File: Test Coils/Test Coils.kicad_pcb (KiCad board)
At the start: 2 copper layers, 71.7 x 64.6 mm, 6 parts, among them J1 Conn_01x02, J2 Conn_01x02, J3 Conn_01x02

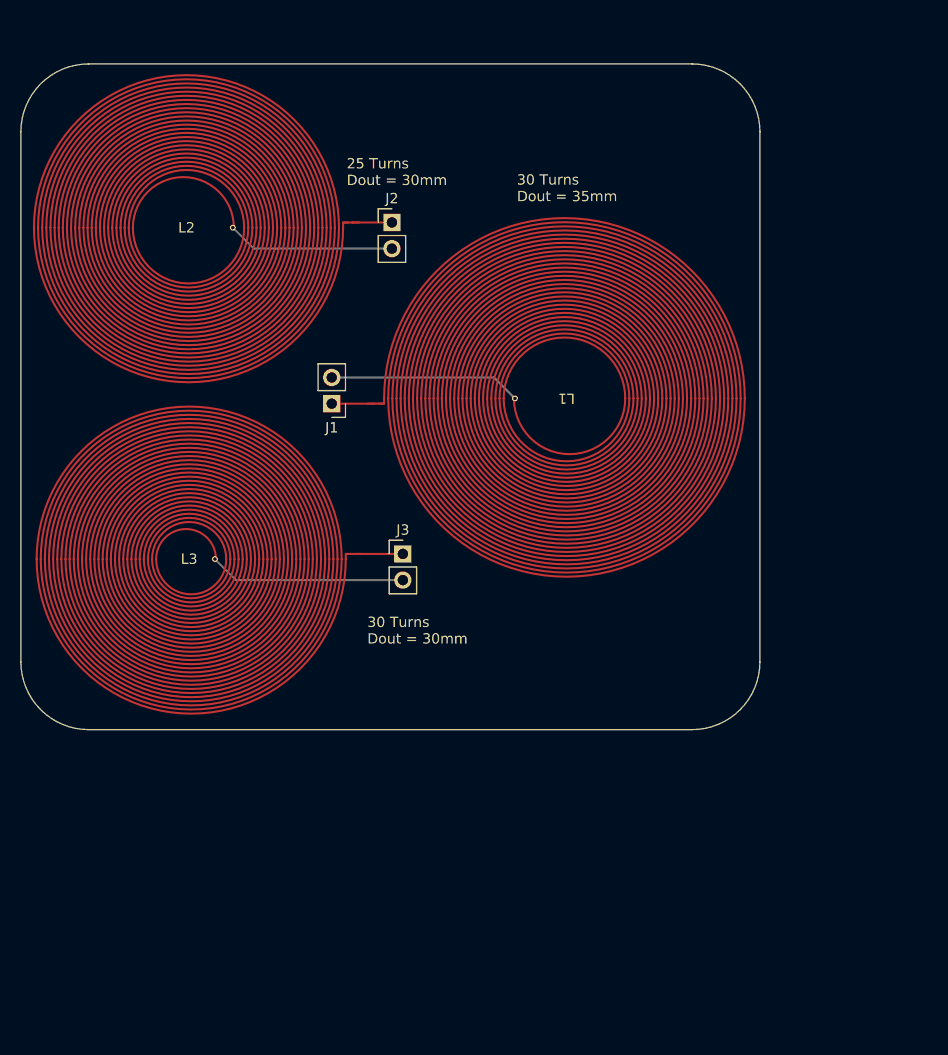
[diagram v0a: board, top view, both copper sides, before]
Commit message: feat(hw): panelizing
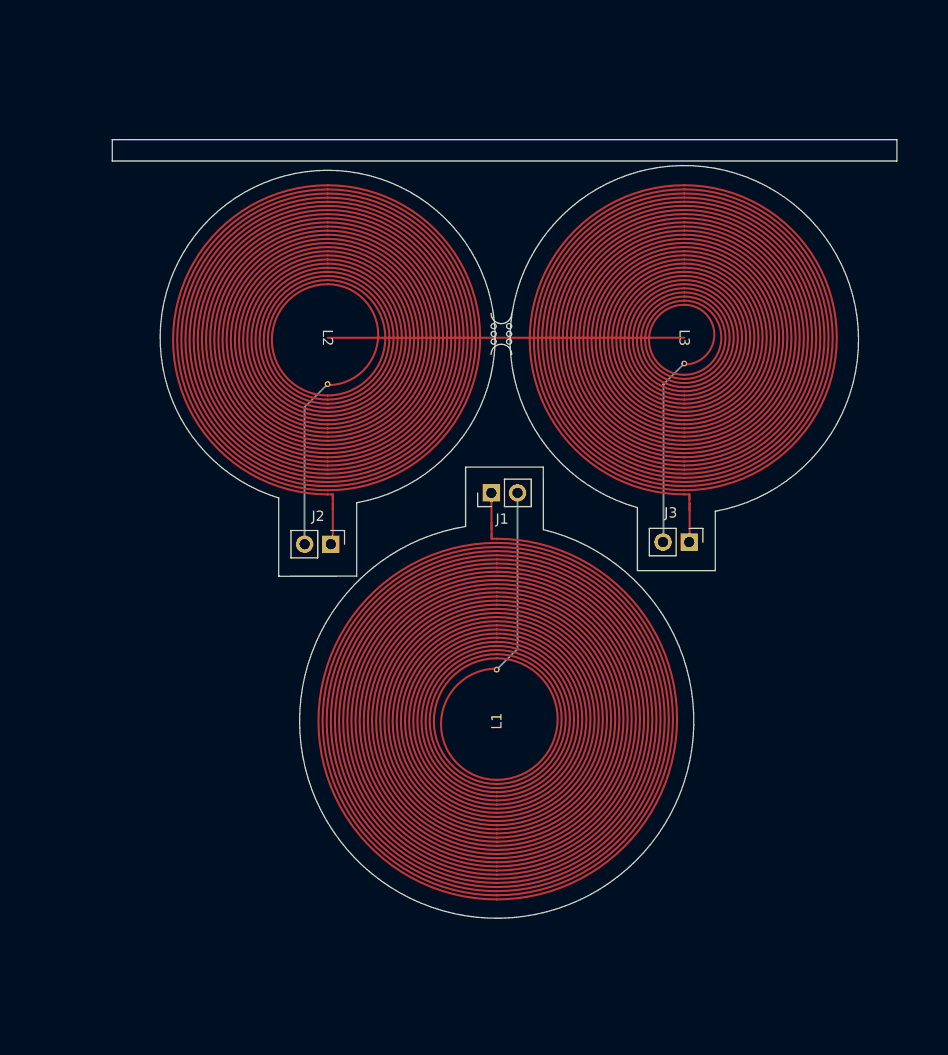
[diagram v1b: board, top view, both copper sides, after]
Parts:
- added mouse-bite-2mm-slot: VAL**, Panelization:mouse-bite-2mm-slot, F.Cu at (60.9, 42.5)
- moved L3 52.6 mm to (78.7, 42.9), turned to -90 degrees
- moved L1 32.0 mm to (60.5, 80.1), turned to 90 degrees
- moved J2 31.8 mm to (44.4, 62.9), turned to -90 degrees
- moved J3 27.8 mm to (79.1, 62.7), turned to -90 degrees
- moved J1 17.7 mm to (59.9, 57.9), turned to 90 degrees
- moved L2 17.4 mm to (44.0, 42.9), turned to -90 degrees
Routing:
- net Net-(J3-Pin_2): track 19.1 -> 18.2 mm
- net Net-(J3-Pin_1): track 4.64 -> 3.76 mm
- net Net-(J1-Pin_1): track 4.17 -> 3.54 mm
- net Net-(J1-Pin_2): track 18.6 -> 18.0 mm
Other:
- board size 71.7 x 64.6 mm -> 76.1 x 75.6 mm

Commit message: fix(hw): change edge cuts
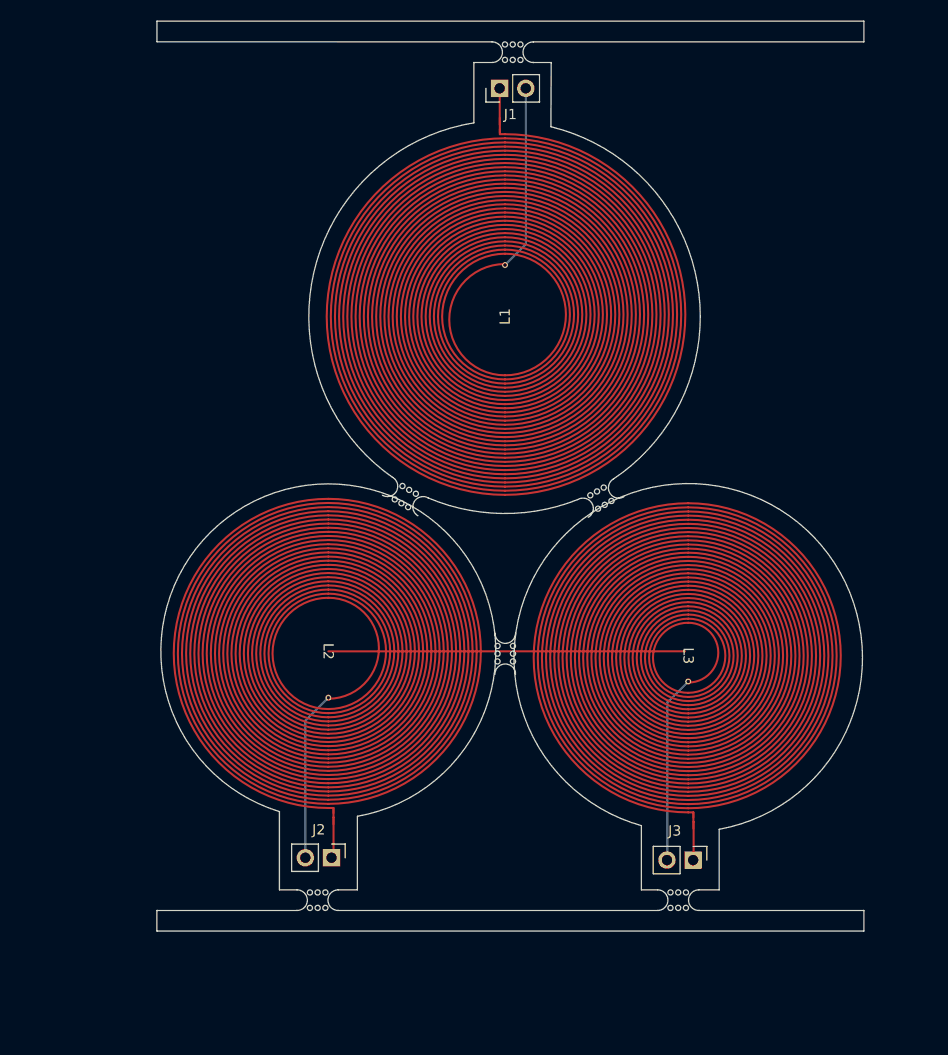
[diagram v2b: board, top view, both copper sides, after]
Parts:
- added mouse-bite-2mm-slot: VAL**, Panelization:mouse-bite-2mm-slot, F.Cu at (43.1, 97.5)
- added mouse-bite-2mm-slot: VAL**, Panelization:mouse-bite-2mm-slot, F.Cu at (70.6, 58.4)
- added mouse-bite-2mm-slot: VAL**, Panelization:mouse-bite-2mm-slot, F.Cu at (62.0, 15.2)
- added mouse-bite-2mm-slot: VAL**, Panelization:mouse-bite-2mm-slot, F.Cu at (51.6, 58.3)
- added mouse-bite-2mm-slot: VAL**, Panelization:mouse-bite-2mm-slot, F.Cu at (78.1, 97.5)
- moved J1 39.3 mm to (60.7, 18.7)
- moved L1 39.3 mm to (61.3, 40.8)
- moved mouse-bite-2mm-slot 31.0 mm to (61.3, 73.5)
- moved L3 30.9 mm to (79.0, 73.7)
- moved J3 30.9 mm to (79.5, 93.6)
- moved J2 30.4 mm to (44.4, 93.3)
- moved L2 30.4 mm to (44.1, 73.3)
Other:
- board size 76.1 x 75.6 mm -> 68.6 x 88.3 mm

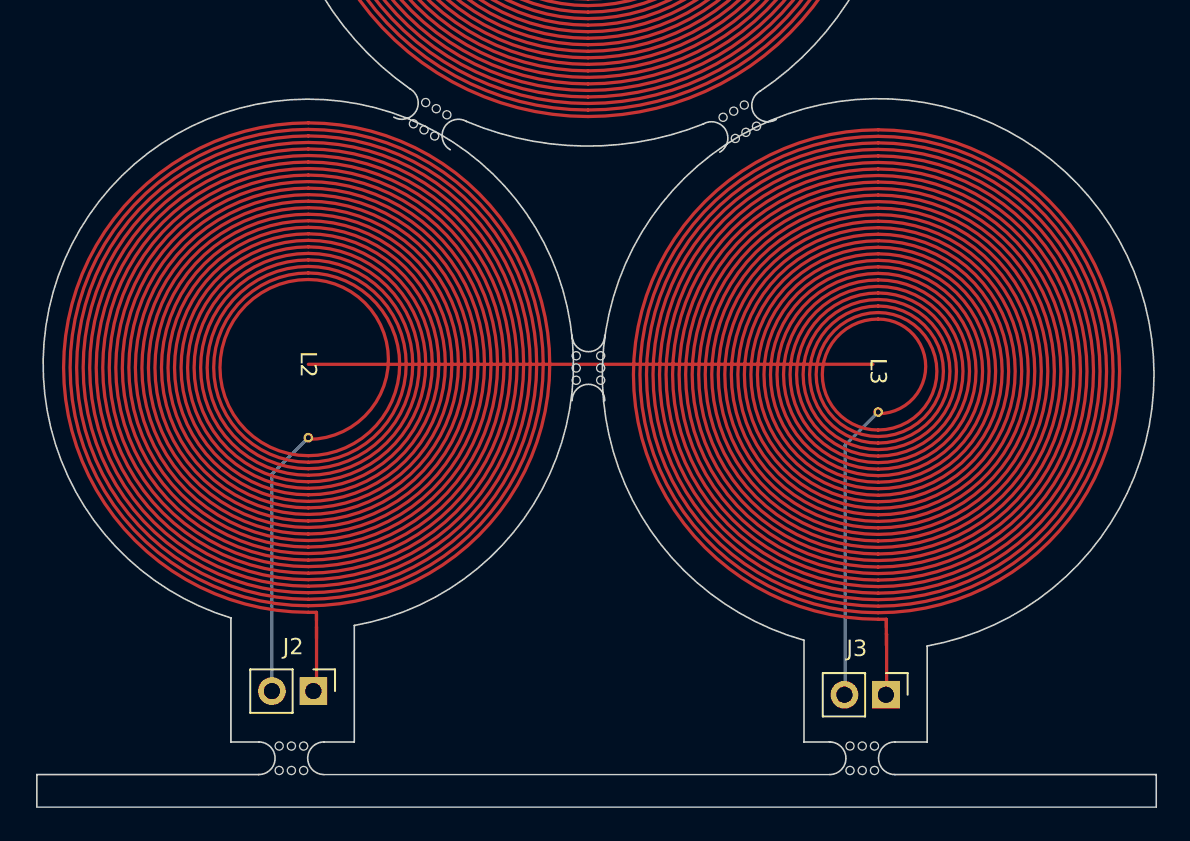
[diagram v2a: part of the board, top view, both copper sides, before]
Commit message: fix(hw): update edge cuts
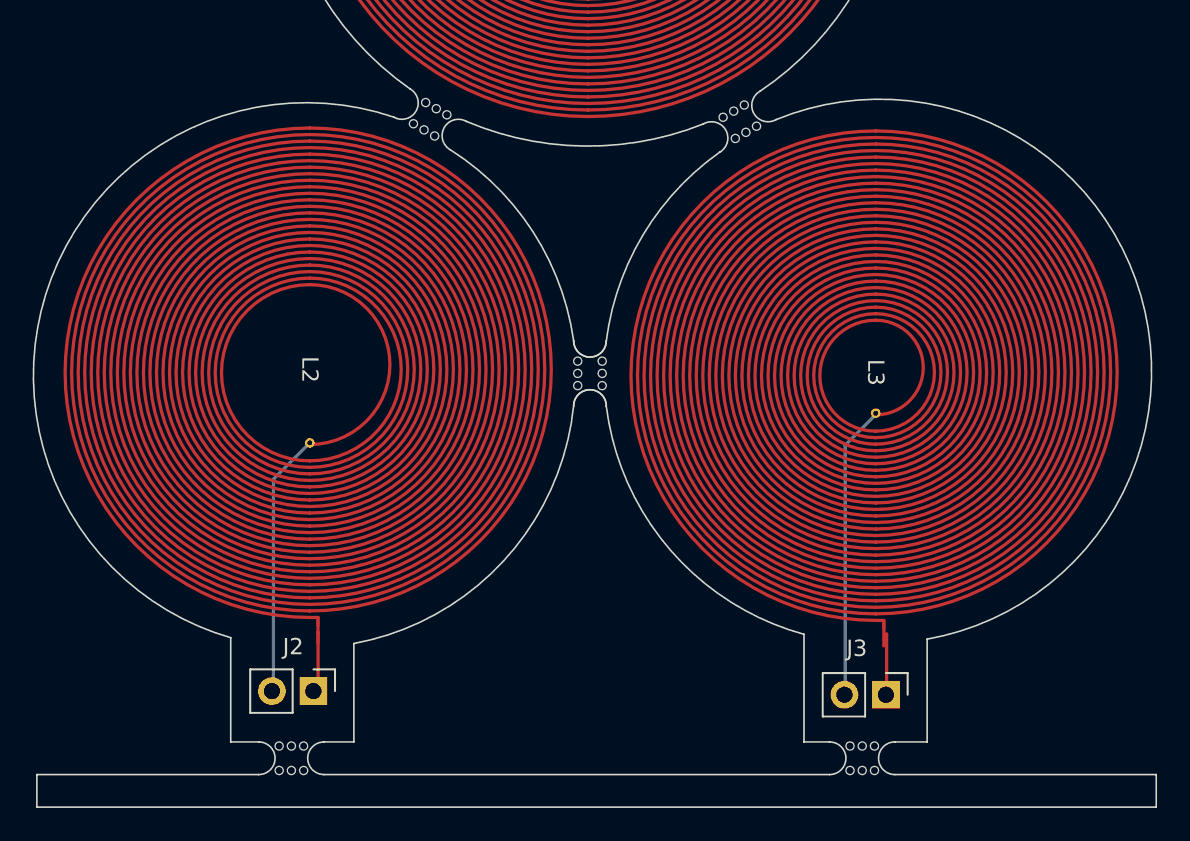
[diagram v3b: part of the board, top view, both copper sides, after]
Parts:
- moved mouse-bite-2mm-slot 0.34 mm to (61.4, 73.9)
- moved L2 0.33 mm to (44.2, 73.6)
- moved L3 0.17 mm to (78.9, 73.8)
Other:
- board size 68.6 x 88.3 mm -> 68.8 x 88.3 mm

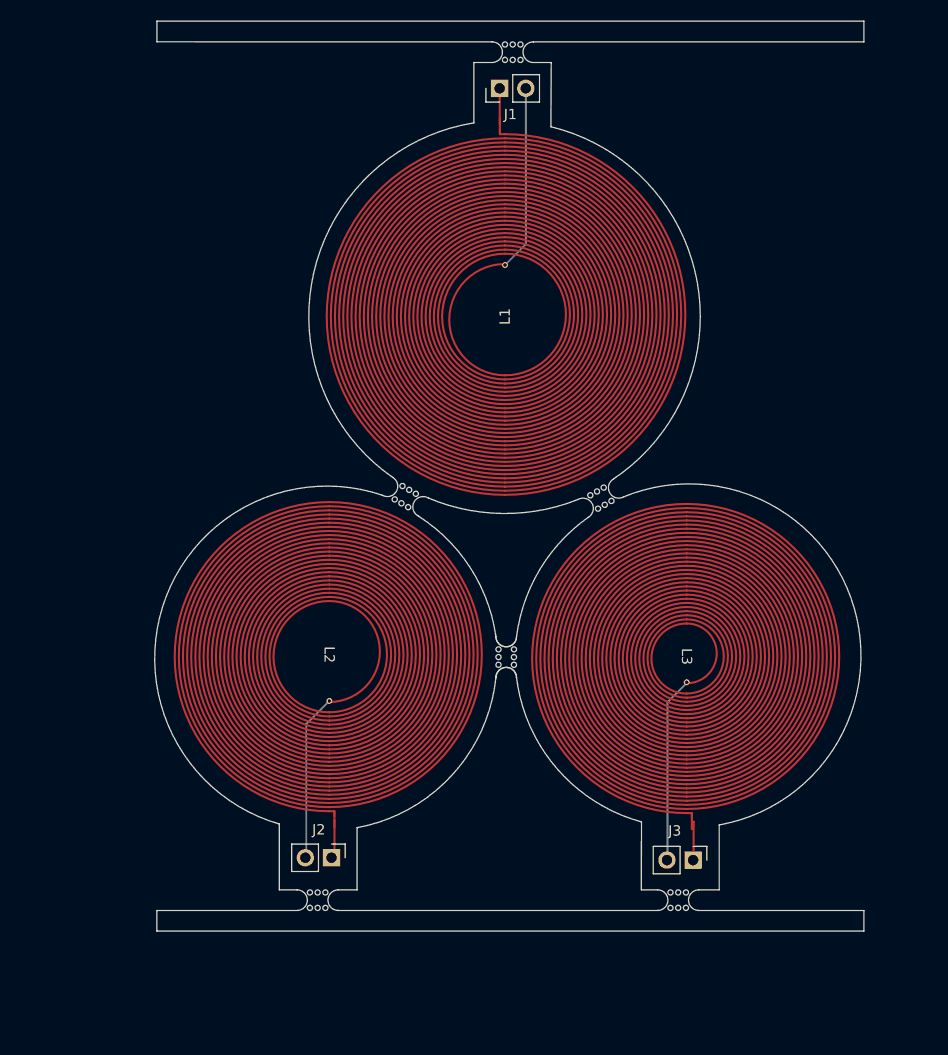
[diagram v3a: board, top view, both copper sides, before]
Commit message: fix(hw): update edge cuts
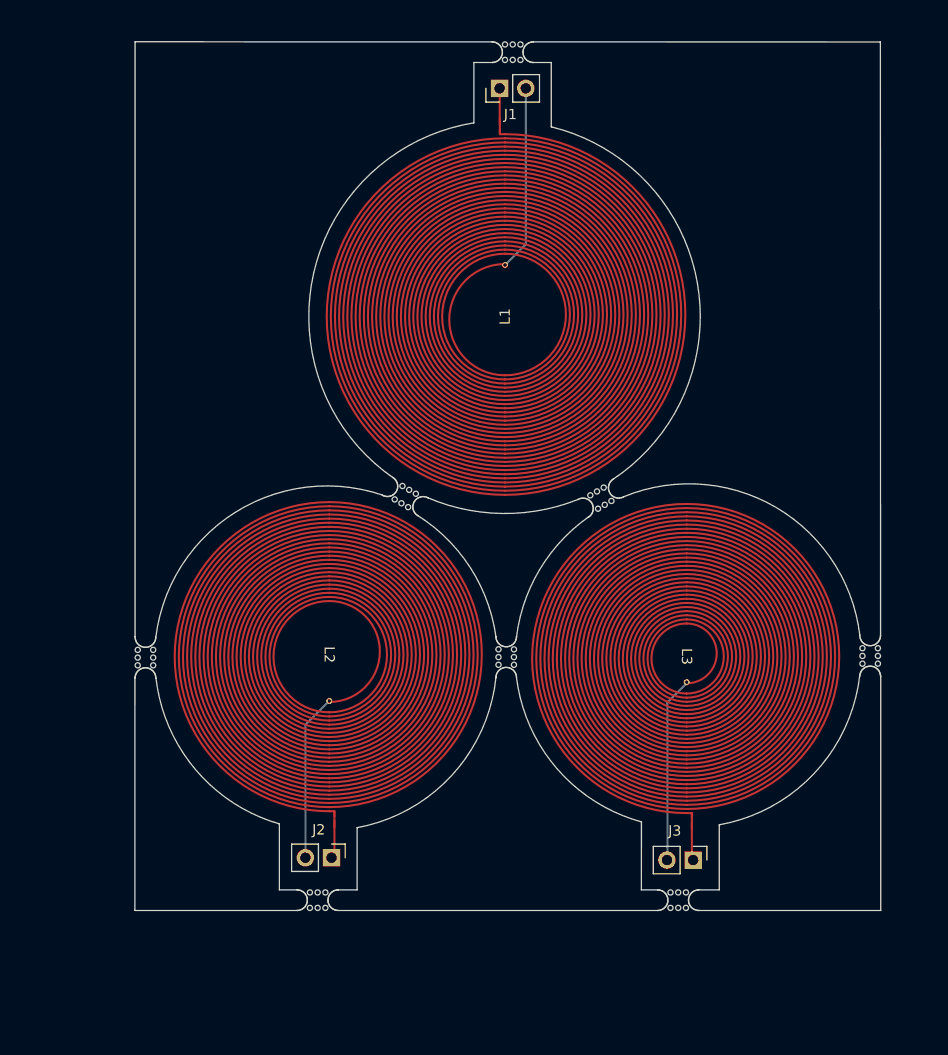
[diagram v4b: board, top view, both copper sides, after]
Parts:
- added mouse-bite-2mm-slot: VAL**, Panelization:mouse-bite-2mm-slot, F.Cu at (26.4, 73.9)
- added mouse-bite-2mm-slot: VAL**, Panelization:mouse-bite-2mm-slot, F.Cu at (96.7, 73.8)
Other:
- board size 68.8 x 88.3 mm -> 72.4 x 84.3 mm

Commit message: fix(hw): panelization changes
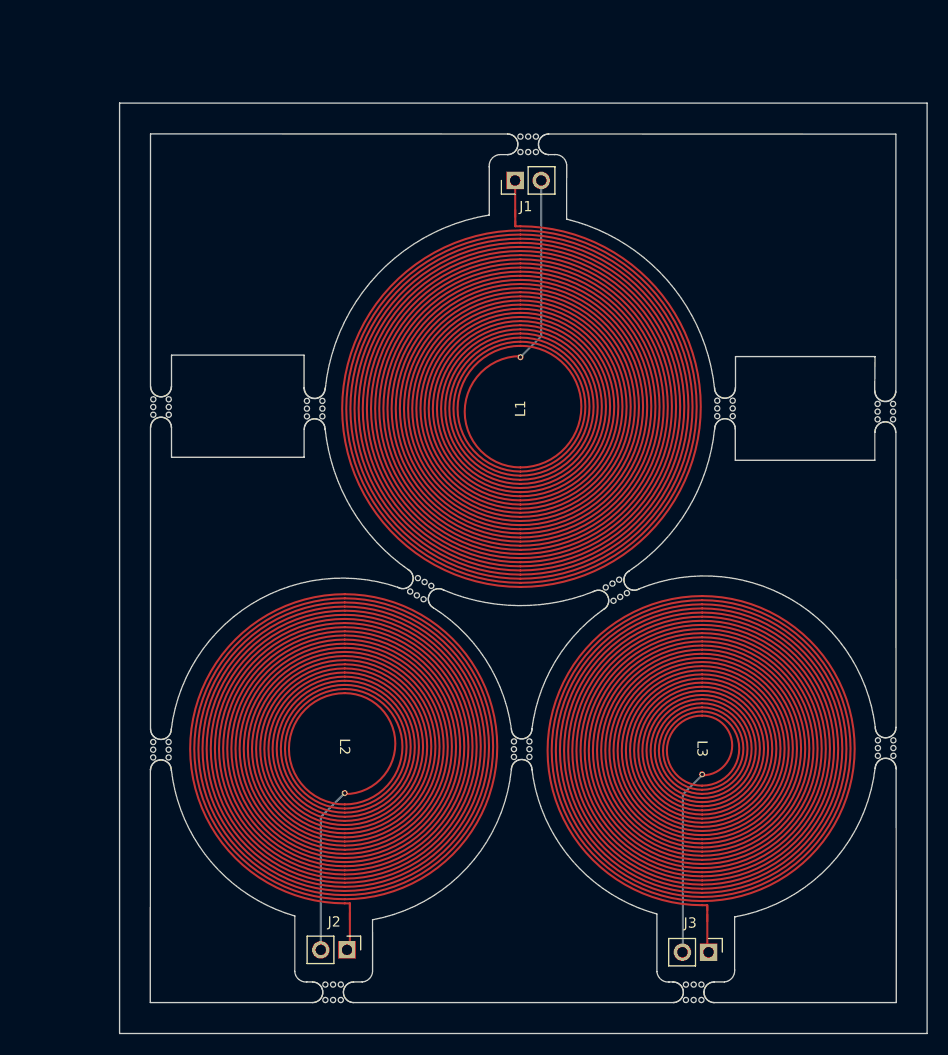
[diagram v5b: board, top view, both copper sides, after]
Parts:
- added mouse-bite-2mm-slot: VAL**, Panelization:mouse-bite-2mm-slot, F.Cu at (98.2, 50.0)
- added mouse-bite-2mm-slot: VAL**, Panelization:mouse-bite-2mm-slot, F.Cu at (42.8, 49.7)
- added mouse-bite-2mm-slot: VAL**, Panelization:mouse-bite-2mm-slot, F.Cu at (82.6, 49.7)
- added mouse-bite-2mm-slot: VAL**, Panelization:mouse-bite-2mm-slot, F.Cu at (27.9, 49.6)
- moved L1 9.06 mm to (62.8, 49.8)
- moved mouse-bite-2mm-slot 9.06 mm to (53.1, 67.2)
- moved J1 9.06 mm to (62.2, 27.6)
- moved J2 9.06 mm to (45.9, 102.3)
- moved J3 9.06 mm to (81.0, 102.5)
- moved L2 9.06 mm to (45.7, 82.6)
- moved L3 9.06 mm to (80.4, 82.7)
- moved mouse-bite-2mm-slot 9.06 mm to (27.9, 82.8)
- moved mouse-bite-2mm-slot 9.06 mm to (79.6, 106.4)
- moved mouse-bite-2mm-slot 9.06 mm to (44.6, 106.4)
- moved mouse-bite-2mm-slot 9.06 mm to (62.9, 82.8)
- moved mouse-bite-2mm-slot 9.06 mm to (63.5, 24.1)
- moved mouse-bite-2mm-slot 9.06 mm to (98.2, 82.7)
- moved mouse-bite-2mm-slot 9.06 mm to (72.1, 67.4)
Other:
- board size 72.4 x 84.3 mm -> 78.4 x 90.3 mm
